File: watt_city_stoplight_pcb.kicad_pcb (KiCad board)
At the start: 2 copper layers, 40.9 x 44 mm, 26 parts, among them J201 USB_C_Receptacle_USB2.0_14P, SW301 Reset, SW302 Boot, SW401 SW_Wuerth_450301014042, U201 SLLC23T5V2U, U301 ESP32-S3-WROOM-1-N8, U401 AP2112K-3.3

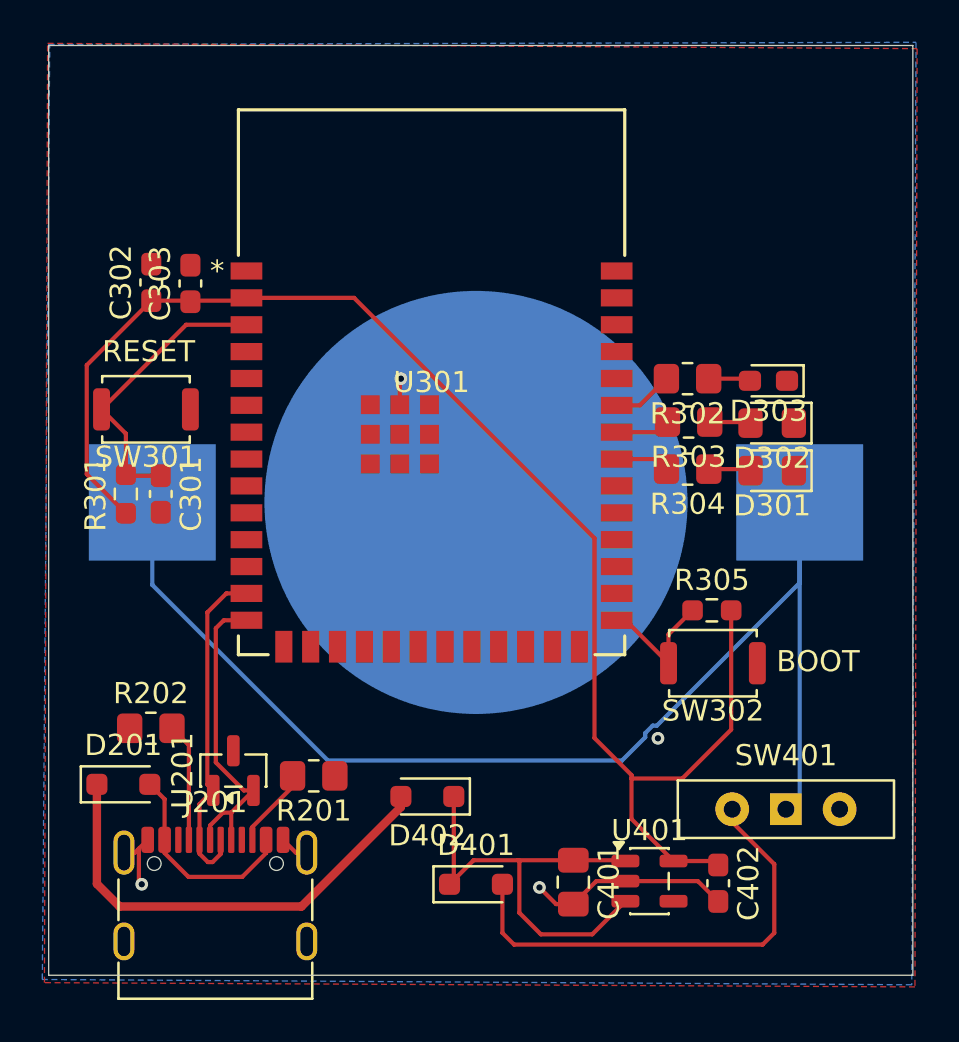
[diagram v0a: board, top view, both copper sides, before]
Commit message: changed layout
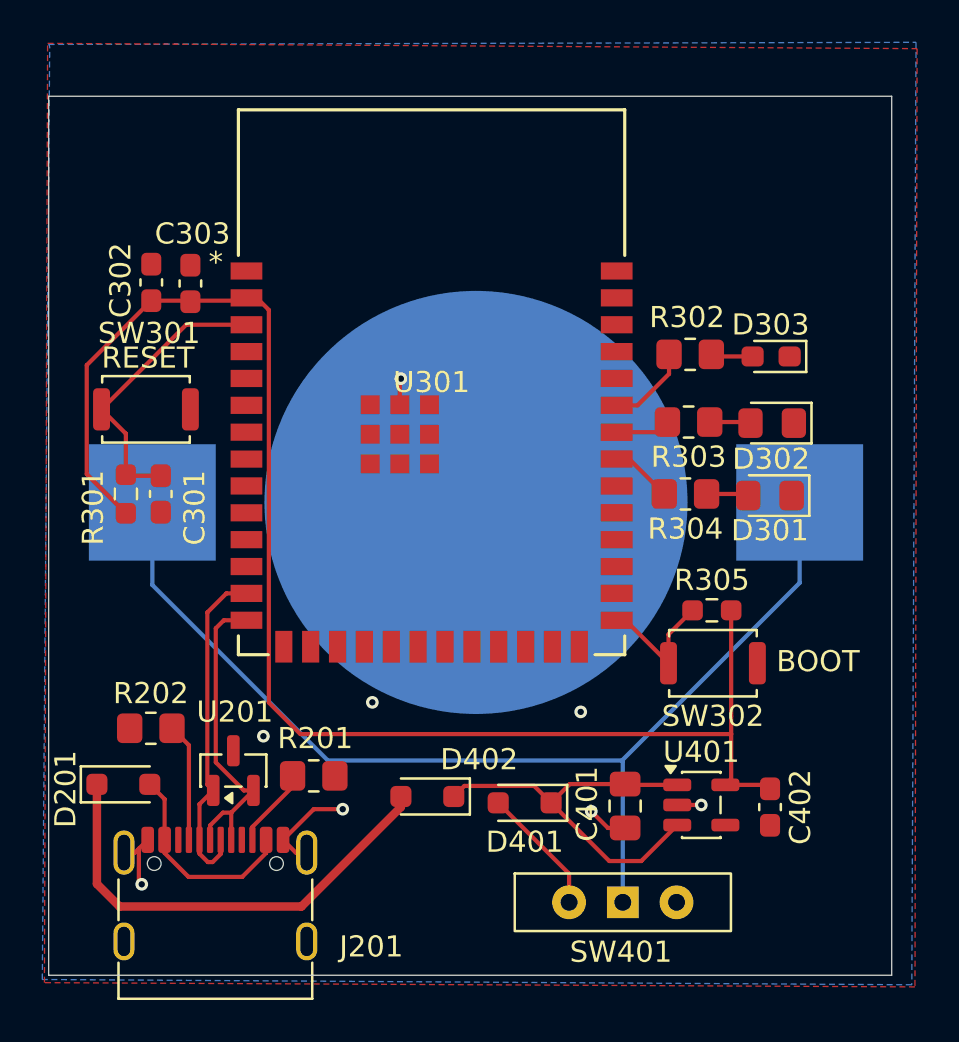
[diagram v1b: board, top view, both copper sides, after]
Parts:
- moved SW401 8.88 mm to (144.1, 110.5)
- moved D401 4.48 mm to (139.4, 105.8), turned to 180 degrees
- moved C402 4.35 mm to (151.1, 106.0)
- moved U401 4.35 mm to (147.8, 105.9)
- moved C401 4.35 mm to (144.2, 106.0)
- moved D301 1.18 mm to (151.0, 91.3)
- moved R304 1.18 mm to (147.1, 91.2)
- moved R302 1.16 mm to (147.3, 84.6)
- moved D303 1.16 mm to (151.1, 84.7)
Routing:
- net Net-(D401-A): track 22.4 -> 6.09 mm
- net GND: track 22.7 -> 12.2 mm, vias 4 -> 8
- net Net-(BT401-+): track 60.1 -> 51.9 mm
- net Net-(D401-K): track 21.3 -> 19.3 mm
- net /mcu/3V3: track 67.6 -> 69.1 mm
- net Net-(U301-IO42): track 2.87 -> 4.02 mm
- net Net-(U301-IO40): track 1.88 -> 2.93 mm
- net Net-(U301-IO41): track 1.92 -> 2.60 mm
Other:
- board size 40.9 x 44 mm -> 39.9 x 41.5 mm

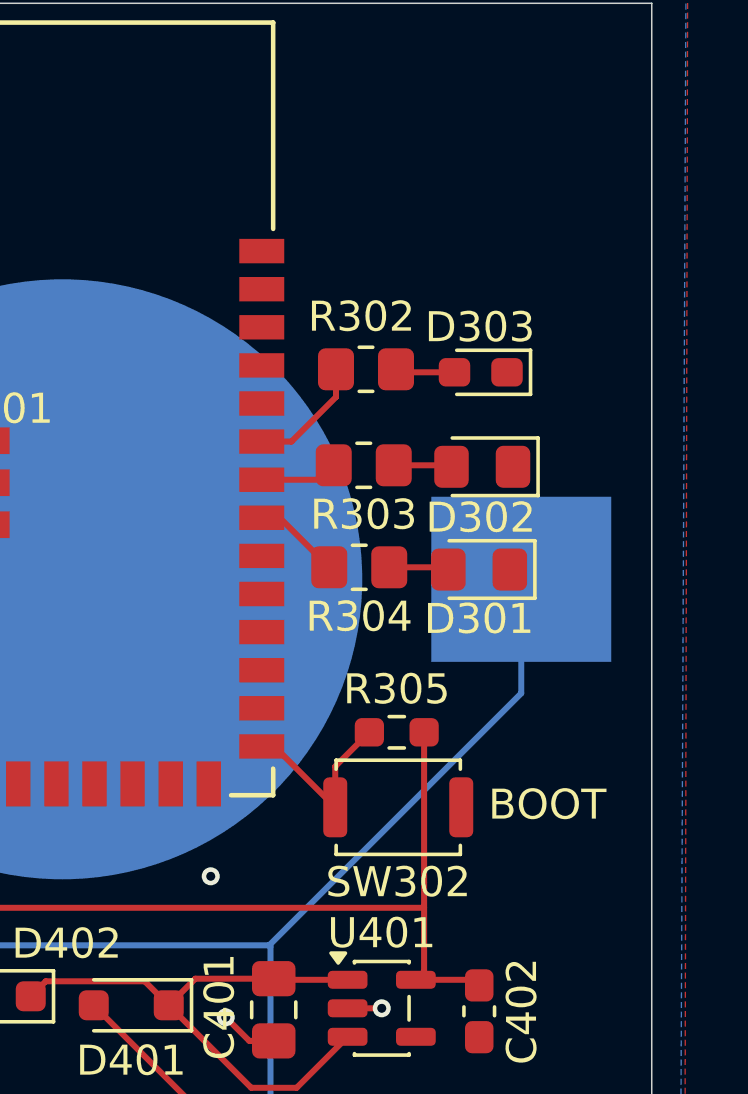
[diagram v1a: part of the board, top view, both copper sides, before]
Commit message: added stoplight button
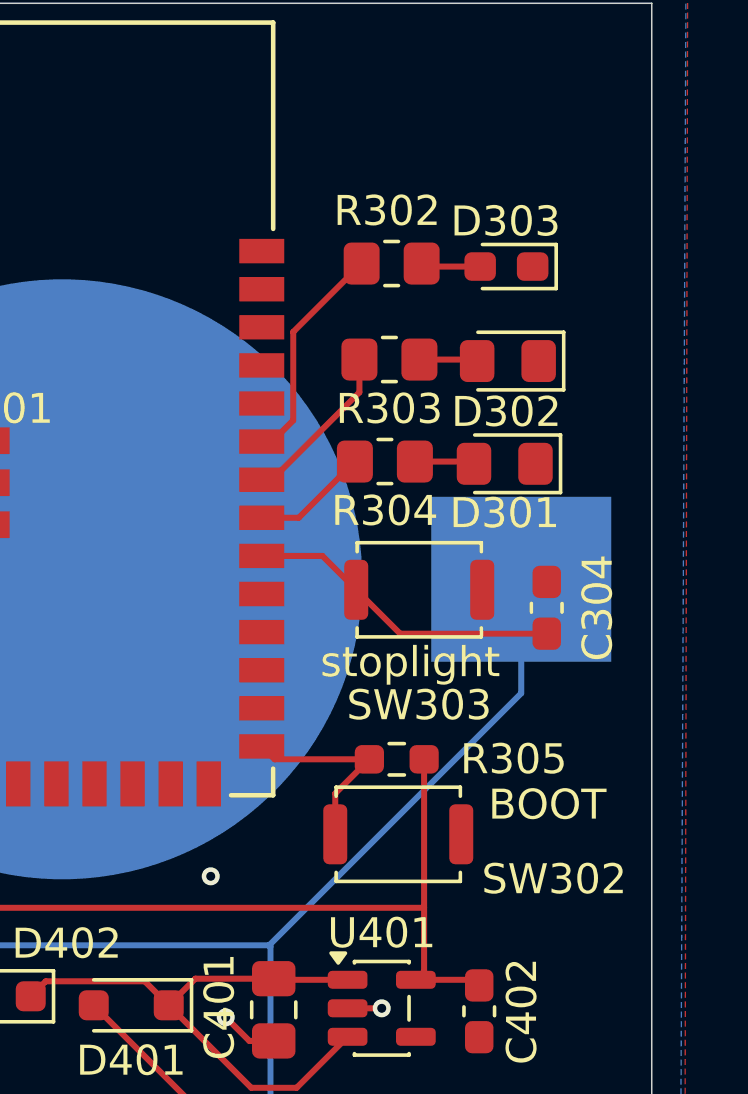
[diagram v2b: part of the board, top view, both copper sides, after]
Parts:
- added C304: 100n, Capacitor_SMD:C_0603_1608Metric_Pad1.08x0.95mm_HandSolder, F.Cu at (153.3, 92.5)
- added SW303: SW, Button_Switch_SMD:SW_Push_SPST_NO_Alps_SKRK, F.Cu at (149.1, 92.0)
- moved D301 3.63 mm to (151.9, 87.8)
- moved D303 3.63 mm to (152.0, 81.2)
- moved R304 3.63 mm to (147.9, 87.7)
- moved R303 3.63 mm to (148.1, 84.3)
- moved D302 3.63 mm to (152.0, 84.3)
- moved R302 3.63 mm to (148.1, 81.1)
- moved R305 0.90 mm to (148.3, 97.6)
- moved SW302 0.90 mm to (148.3, 100.1)
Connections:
- U301 pad 32: unconnected-(U301-IO39-Pad32) -> Net-(U301-IO39)
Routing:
- net Net-(U301-IO39): track 0.00 -> 10.6 mm
- net Net-(U301-IO41): track 2.60 -> 6.23 mm
- net Net-(U301-IO42): track 4.02 -> 7.52 mm
- net Net-(U301-IO40): track 2.93 -> 3.88 mm
- net /mcu/3V3: track 69.1 -> 68.2 mm
- net Net-(U301-IO0): track 5.84 -> 6.74 mm
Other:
- board text added: "stoplight"
